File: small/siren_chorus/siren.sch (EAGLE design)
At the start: 50 parts, among them IC1 NE5532, IC2 PT2399, Q1 J112

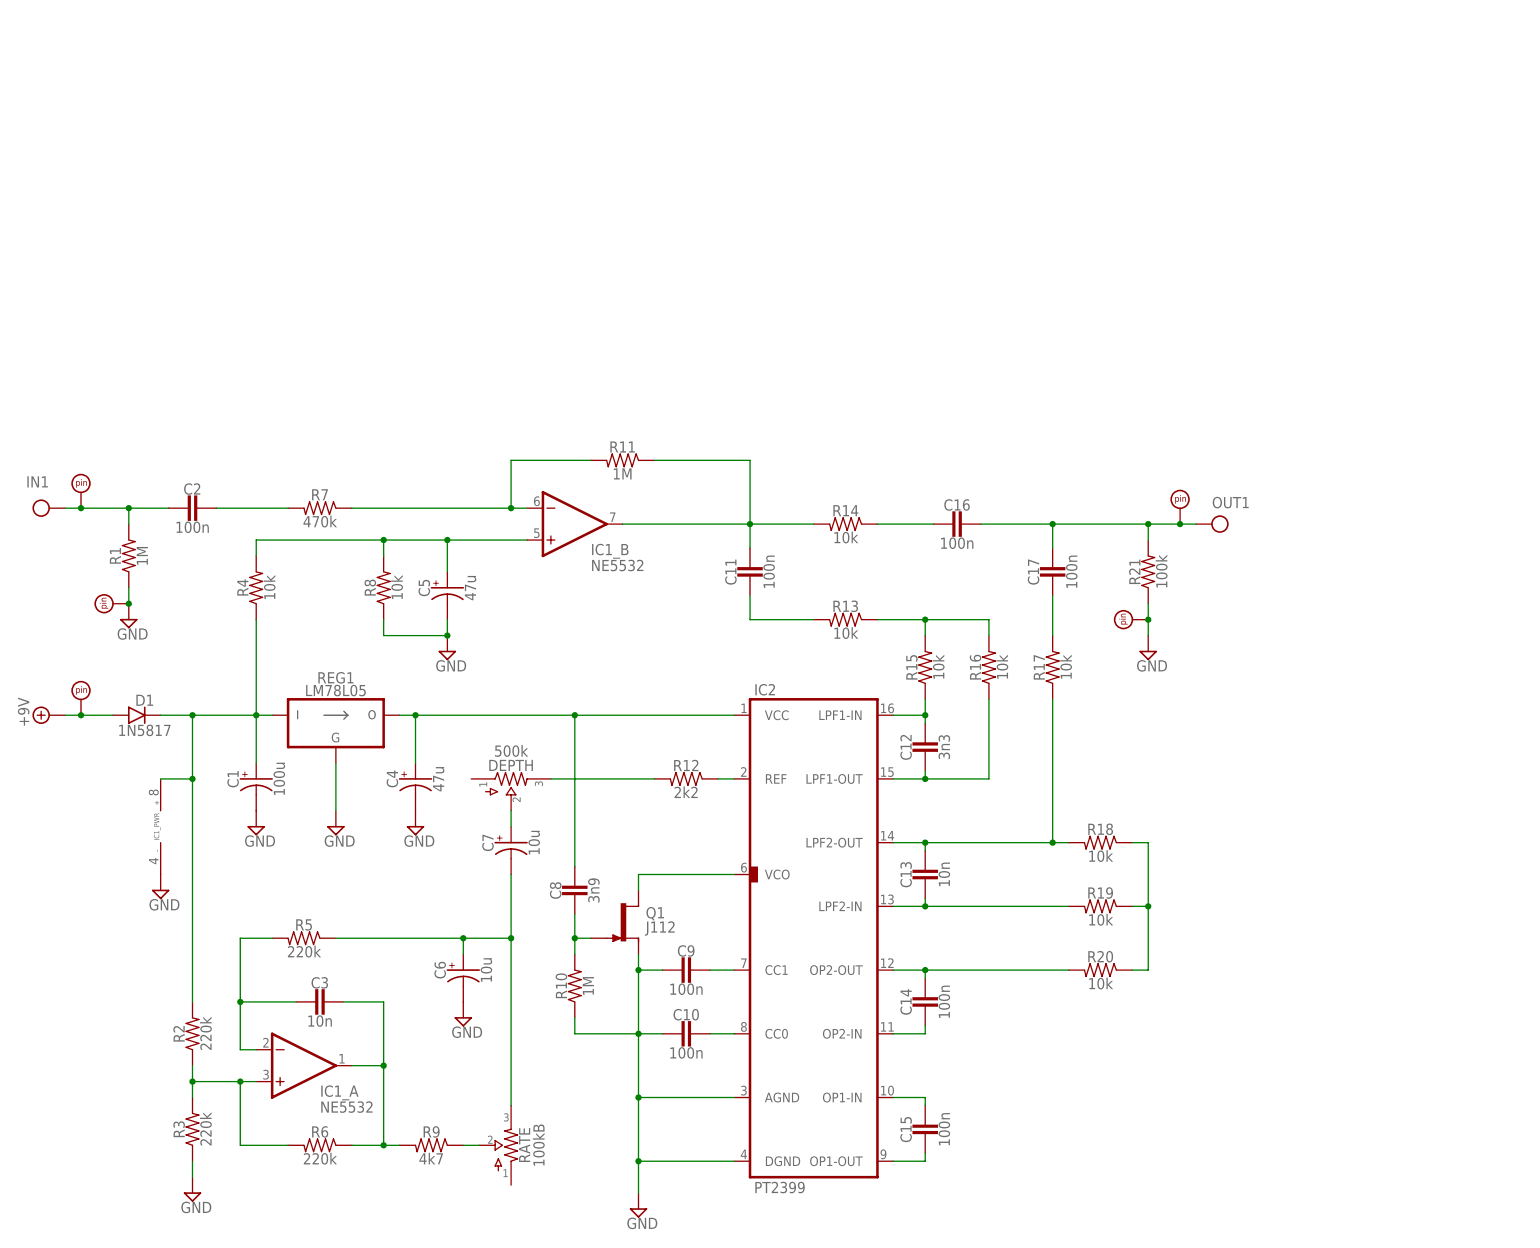
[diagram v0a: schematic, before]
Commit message: add EAGLE library, update 1590a chorus and tremolo, other minor edits
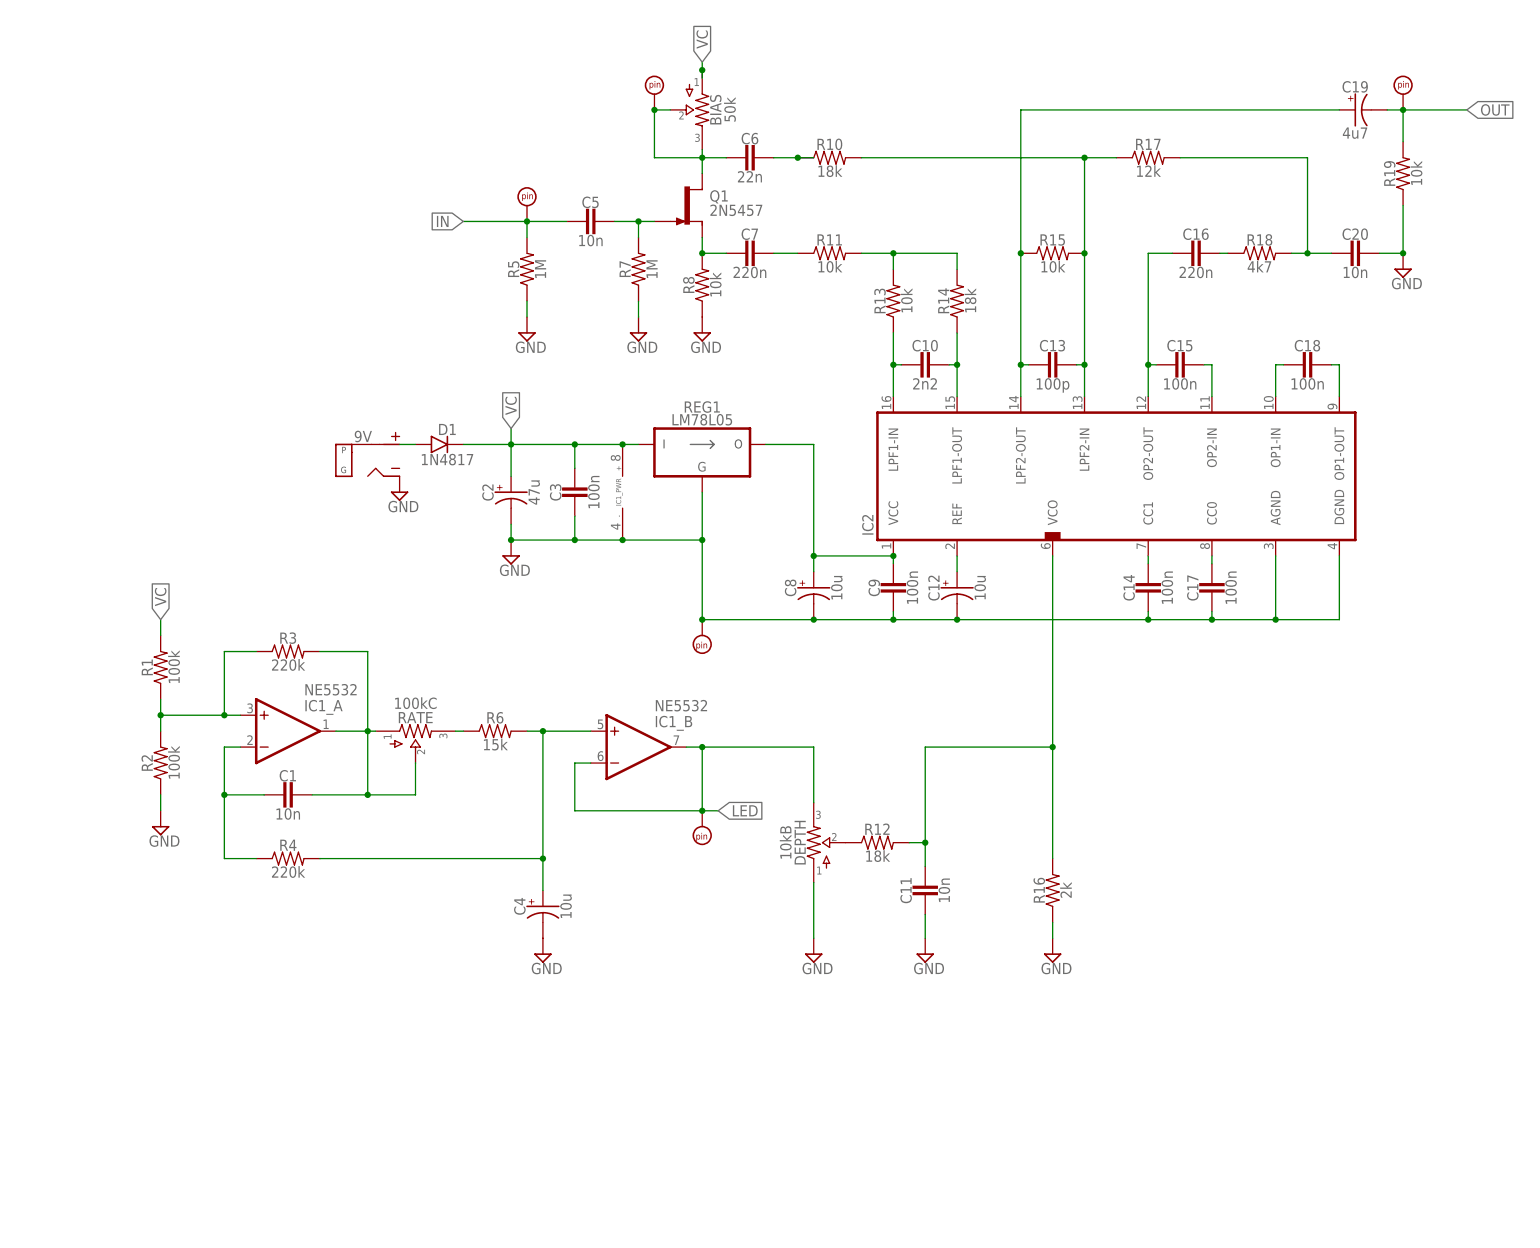
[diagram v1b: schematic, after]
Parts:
- removed PAD1, PAD5: PADSQR, supply pins:PADSQR
- removed PAD3, PAD4: PADRND, supply pins:PADRND
- removed R20: 10k, resistors:R_.2
- removed R21: 100k, resistors:R_.2
- removed R9: 4k7, resistors:R_.2
- added 9V: DC_MONO, jacks:DC_MONO
- added BIAS: 50k, potentiometers:POTSTRIM
- added C18: 100n, capacitors-film:CER/FILM2
- added C19: 4u7, capacitors-elec:0501
- added C20: 10n, capacitors-film:CER/FILM2
- added GND: PADRND, supply pins:PADRND
- added IN, LED, OUT: PADSQR, supply pins:PADSQR
- C1: value 100u -> 10n; device capacitors-elec:0501 -> capacitors-film:CER/FILM2
- C10: value 100n -> 2n2; device capacitors-film:CER/FILMBOX.1 -> capacitors-film:CER/FILM2
- C11: value 100n -> 10n; device capacitors-film:CER/FILMBOX.1 -> capacitors-film:CER/FILM2
- C12: value 3n3 -> 10u; device capacitors-film:CER/FILMBOX.1 -> capacitors-elec:0501
- C13: value 10n -> 100p; device capacitors-film:CER/FILMBOX.1 -> capacitors-film:CER/FILM2
- C14, C15, C17, C9: device capacitors-film:CER/FILMBOX.1 -> capacitors-film:CER/FILM2
- C16: value 100n -> 220n; device capacitors-film:CER/FILMBOX.1 -> capacitors-film:CER/FILM2
- C2: value 100n -> 47u; device capacitors-film:CER/FILMBOX.1 -> capacitors-elec:0501
- C3: value 10n -> 100n; device capacitors-film:CER/FILMBOX.1 -> capacitors-film:CER/FILM2
- C4: value 47u -> 10u
- C5: value 47u -> 10n; device capacitors-elec:0501 -> capacitors-film:CER/FILM2
- C6: value 10u -> 22n; device capacitors-elec:0501 -> capacitors-film:CER/FILM2
- C7: value 10u -> 220n; device capacitors-elec:0501 -> capacitors-film:CER/FILM2
- C8: value 3n9 -> 10u; device capacitors-film:CER/FILMBOX.1 -> capacitors-elec:0500
- D1: value 1N5817 -> 1N4817; device diodes:DO41.2 -> diodes:DO41.3
- DEPTH: value 500k -> 10kB; device potentiometers:POTSTRIM -> potentiometers:POTSSMALL_PADS
- IC2: value PT2399 -> (none)
- PAD2: value PADSQR -> PAD; device supply pins:PADSQR -> supply pins:PAD
- Q1: value J112 -> 2N5457
- R1: value 1M -> 100k
- R10: value 1M -> 18k
- R11: value 1M -> 10k
- R12: value 2k2 -> 18k
- R14: value 10k -> 18k
- R16: value 10k -> 2k
- R17: value 10k -> 12k
- R18: value 10k -> 4k7
- R2: value 220k -> 100k
- R4: value 10k -> 220k
- R5: value 220k -> 1M
- R6: value 220k -> 15k
- R7: value 470k -> 1M
- RATE: value 100kB -> 100kC
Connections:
- removed net N$1: C12.1, IC2.LPF1-IN, R15.1
- removed net N$2: C12.2, IC2.LPF1-OUT, R16.1
- removed net N$29: R9.1, RATE.2
- removed net N$30: C3.1, IC1_A.OUT, R6.1, R9.2
- removed net N$32: C1.+, D1.C, IC1_PWR.V+, R2.2, R4.1, REG1.VI
- new net LED: DEPTH.3, IC1_B.-IN, IC1_B.OUT, LED.P$1
- new net N$27: R6.1, RATE.3
- new net VC: BIAS.1, C2.+, C3.1, D1.C, IC1_PWR.V+, R1.2, REG1.VI
- net +9V: now also 9V.TIP; no longer PAD2.P$1
- net GND: now also 9V.SLEEVE, C11.2, C12.-, C14.2, C17.2, C2.-, C20.1, C3.2, C8.-, DEPTH.1, GND.P$1, R16.1, R19.1, R2.1, R5.1, R7.1; no longer C1.-, C10.2, C5.-, C6.-, PAD3.P$1, PAD4.P$1, Q1.S, R1.1, R10.1, R21.1, R3.1
- net IN: now also C5.2, IN.P$1, R5.2; no longer C2.2, PAD1.P$1, R1.2
- net N$10: now also IC2.OP2-IN; no longer IC2.OP1-IN
- net N$11: now also C18.2, IC2.OP1-IN; no longer C15.2, IC2.OP1-OUT
- net N$12: now also C18.1, IC2.OP1-OUT; no longer C17.2, R17.2
- net N$13: now also C13.2, C19.+, IC2.LPF2-OUT, R15.1; no longer C16.2, R14.1
- net N$14: now also C13.1, IC2.LPF2-IN, R10.2, R15.2, R17.1; no longer C11.1, IC1_B.OUT, R11.1, R14.2
- net N$15: now also R13.2, R14.2; no longer IC1_B.-IN, R7.1
- net N$16: now also C7.1, R11.1; no longer C2.1, R7.2
- net N$17: now also C7.2, Q1.S, R8.2; no longer C11.2, R13.2
- net N$18: now also C6.1, R10.1; no longer C5.+, IC1_B.+IN, R4.2, R8.2
- net N$19: now also BIAS.2, BIAS.3, C6.2, PAD2.P$1, Q1.D; no longer C4.+, C8.1, IC2.VCC, REG1.VO
- net N$20: now also C5.1, Q1.G, R7.2; no longer IC2.REF, R12.1
- net N$21: now also IC1_A.+IN, R1.1, R2.2, R3.1; no longer IC2.VCO, Q1.D
- net N$22: now also C15.2, C16.2, IC2.OP2-OUT; no longer C7.+, DEPTH.2
- net N$23: now also C16.1, R18.1; no longer C9.1, IC2.CC1
- net N$24: now also C1.1, IC1_A.OUT, R3.2, RATE.1, RATE.2; no longer C10.1, IC2.CC0
- net N$25: now also C1.2, IC1_A.-IN, R4.1; no longer IC1_A.+IN, R2.1, R3.2, R6.2
- net N$26: now also DEPTH.2, R12.1; no longer C3.2, IC1_A.-IN, R5.2
- net N$28: now also C4.+, IC1_B.+IN, R4.2, R6.2; no longer C6.+, C7.-, R5.1, RATE.3
- net N$3: now also C8.+, C9.1, IC2.VCC, REG1.VO; no longer DEPTH.3, R12.2
- net N$31: now also C11.1, IC2.VCO, R12.2, R16.2; no longer C8.2, Q1.G, R10.2
- net N$4: now also C10.2, IC2.LPF1-IN; no longer R15.2, R16.2
- net N$5: now also C10.1, IC2.LPF1-OUT, R14.1; no longer C13.1, IC2.LPF2-OUT, R17.1, R18.2
- net N$6: now also C20.2, R17.2, R18.2; no longer C14.1, IC2.OP2-OUT, R20.2
- net N$7: now also C12.+, IC2.REF; no longer C13.2, IC2.LPF2-IN, R19.2
- net N$8: now also C14.1, IC2.CC1; no longer R18.1, R19.1, R20.1
- net N$9: now also C17.1, IC2.CC0; no longer C14.2, IC2.OP2-IN
- net OUT: now also C19.-, OUT.P$1, R19.2; no longer C16.1, C17.1, PAD5.P$1, R21.2
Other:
- moved on the sheet: C10, C11, C13, C14, C15, C16, C17, C3, C4, C9, D1, DEPTH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
